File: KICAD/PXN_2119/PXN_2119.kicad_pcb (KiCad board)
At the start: 2 copper layers, 133.5 x 35.2 mm, 94 parts, among them P1 HDR-IDC-2.54-2X3P, P2 SWD, SW1 TS-1187A-B-A-B, U2 SN74HC165N, U3 Micro USB-B 5P_C40942, U4 SN74HC165N, U5 SN74HC165N, U6 SN74HC165N, U7 STM32F103C8T6, U8 AMS1117-3.3, X2 8MHz, X3 32.768kHz

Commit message: Fixing Routing
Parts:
- removed mouse-bite-1mm-slot: VAL**, footprints:mouse-bite-1mm-slot
- added G***: LOGO, LOGO, B.Cu at (104.7, 97.9)
- moved mouse-bite-1mm-slot-1 1.87 mm to (162.7, 113.5)
- moved mouse-bite-1mm-slot-10 1.87 mm to (162.7, 86.1)
- moved mouse-bite-1mm-slot-2 1.87 mm to (162.7, 110.5)
- moved mouse-bite-1mm-slot-11 1.87 mm to (162.7, 83.0)
- moved mouse-bite-1mm-slot-3 1.87 mm to (162.7, 107.4)
- moved mouse-bite-1mm-slot-4 1.87 mm to (162.7, 104.4)
- moved mouse-bite-1mm-slot-5 1.87 mm to (162.7, 101.3)
- moved mouse-bite-1mm-slot-6 1.87 mm to (162.7, 98.3)
- moved mouse-bite-1mm-slot-7 1.87 mm to (162.7, 95.2)
- moved mouse-bite-1mm-slot-8 1.87 mm to (162.7, 92.3)
- moved mouse-bite-1mm-slot-9 1.87 mm to (162.7, 89.2)
- renumbered mouse-bite-1mm-slot to mouse-bite-1mm-slot-1, mouse-bite-1mm-slot to mouse-bite-1mm-slot-10, mouse-bite-1mm-slot to mouse-bite-1mm-slot-11, mouse-bite-1mm-slot to mouse-bite-1mm-slot-2, mouse-bite-1mm-slot to mouse-bite-1mm-slot-3, mouse-bite-1mm-slot to mouse-bite-1mm-slot-4, mouse-bite-1mm-slot to mouse-bite-1mm-slot-5, mouse-bite-1mm-slot to mouse-bite-1mm-slot-6, mouse-bite-1mm-slot to mouse-bite-1mm-slot-7, mouse-bite-1mm-slot to mouse-bite-1mm-slot-8, mouse-bite-1mm-slot to mouse-bite-1mm-slot-9
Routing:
- net GND: track 385.4 -> 455.8 mm, vias 3 -> 4
- net PB6: track 48.3 -> 82.2 mm
- net /VCC_THR: track 123.6 -> 100.5 mm
- net PA8: track 45.4 -> 24.0 mm
- net PB4: track 50.7 -> 67.1 mm, vias 2 -> 1
- net VCC: track 297.6 -> 313.6 mm, vias 2 -> 4
- net Net-(H1-Pad8): track 34.6 -> 19.1 mm
- net PB8: track 28.9 -> 18.1 mm
- net PB5: track 48.6 -> 58.3 mm, vias 0 -> 2
- net Net-(H4-Pad1): track 5.56 -> 14.4 mm
- net Net-(H10-Pad8): track 5.00 -> 13.4 mm
- net Net-(H10-Pad4): track 35.5 -> 27.5 mm, vias 0 -> 1
- net SWCLK: track 32.7 -> 25.6 mm
- net Net-(H1-Pad2): track 17.2 -> 24.3 mm
- net BOOT0: track 19.3 -> 26.3 mm
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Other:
- board size 133.5 x 35.2 mm -> 133.8 x 35.1 mm

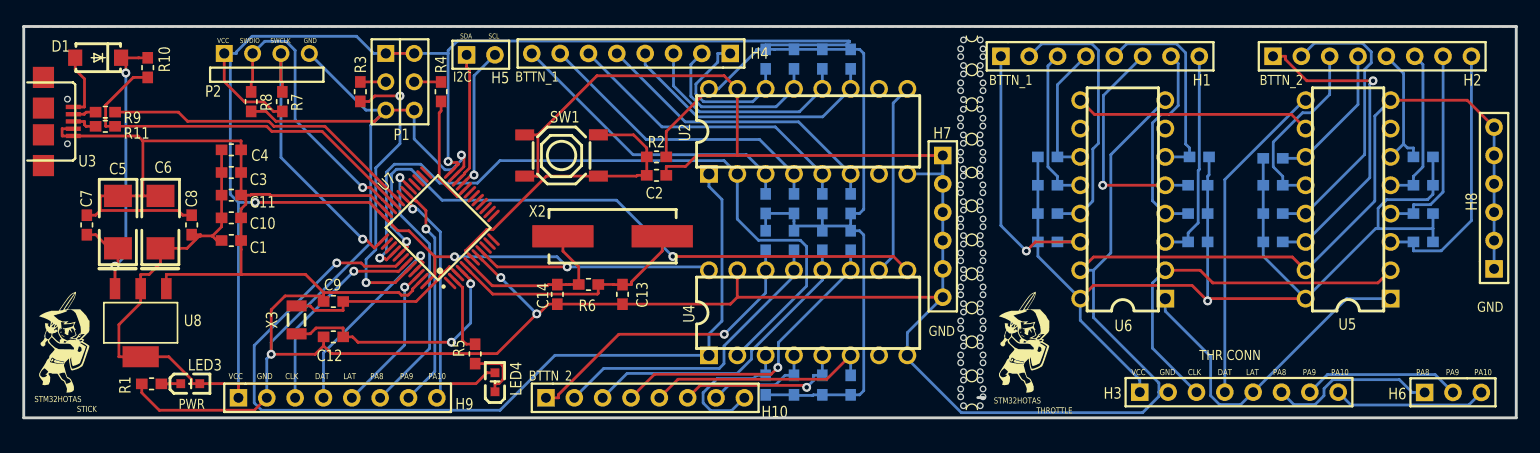
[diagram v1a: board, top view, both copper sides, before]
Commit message: updating pcb
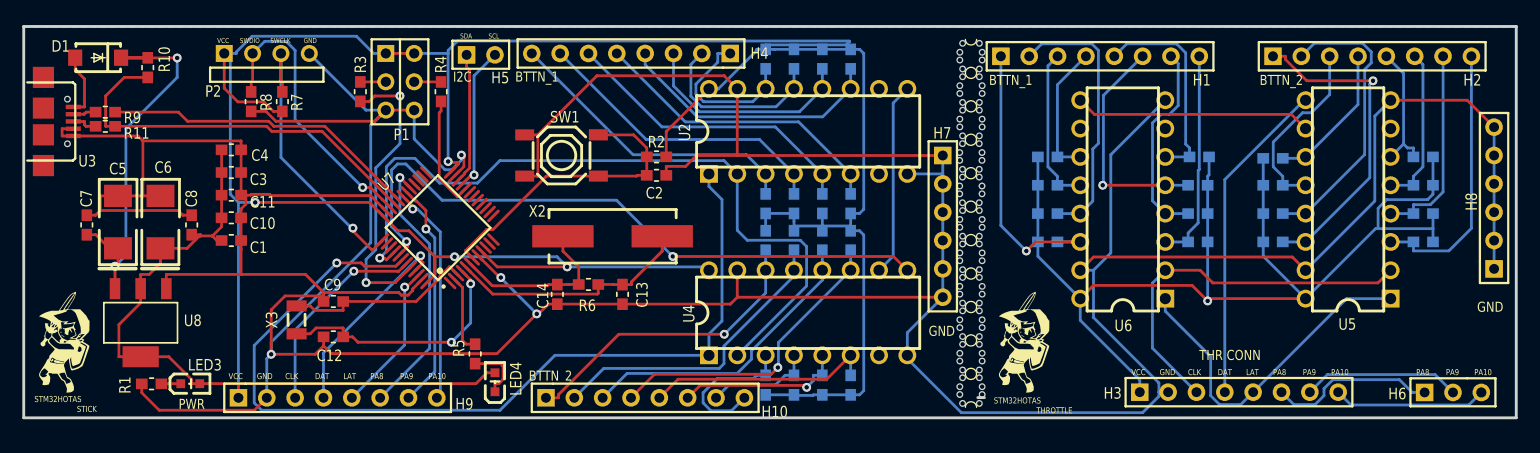
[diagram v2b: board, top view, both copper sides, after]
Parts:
- moved mouse-bite-1mm-slot-11 0.31 mm to (162.6, 83.3)
- moved mouse-bite-1mm-slot-10 0.26 mm to (162.6, 86.3)
- moved mouse-bite-1mm-slot-1 0.22 mm to (162.6, 113.3)
- moved mouse-bite-1mm-slot-2 0.17 mm to (162.6, 110.3)
- moved mouse-bite-1mm-slot-3 0.13 mm to (162.6, 107.3)
- moved mouse-bite-1mm-slot-7 0.13 mm to (162.6, 95.3)
- moved mouse-bite-1mm-slot-9 0.11 mm to (162.6, 89.3)
- moved mouse-bite-1mm-slot-4 0.09 mm to (162.6, 104.3)
- moved mouse-bite-1mm-slot-6 0.09 mm to (162.6, 98.3)
- moved mouse-bite-1mm-slot-8 0.08 mm to (162.6, 92.3)
- moved mouse-bite-1mm-slot-5 0.08 mm to (162.6, 101.3)
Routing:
- net +5V: track 28.8 -> 35.3 mm
- net PB4: track 67.1 -> 68.4 mm
- net PB5: track 58.3 -> 58.9 mm
